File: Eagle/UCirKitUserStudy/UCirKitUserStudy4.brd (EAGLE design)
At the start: 104.1 x 146.3 mm, 30 parts, among them IC1 74595DIL16-OVAL-PIN, IC2 LM35TO92-EXPANDED-OVAL-PIN

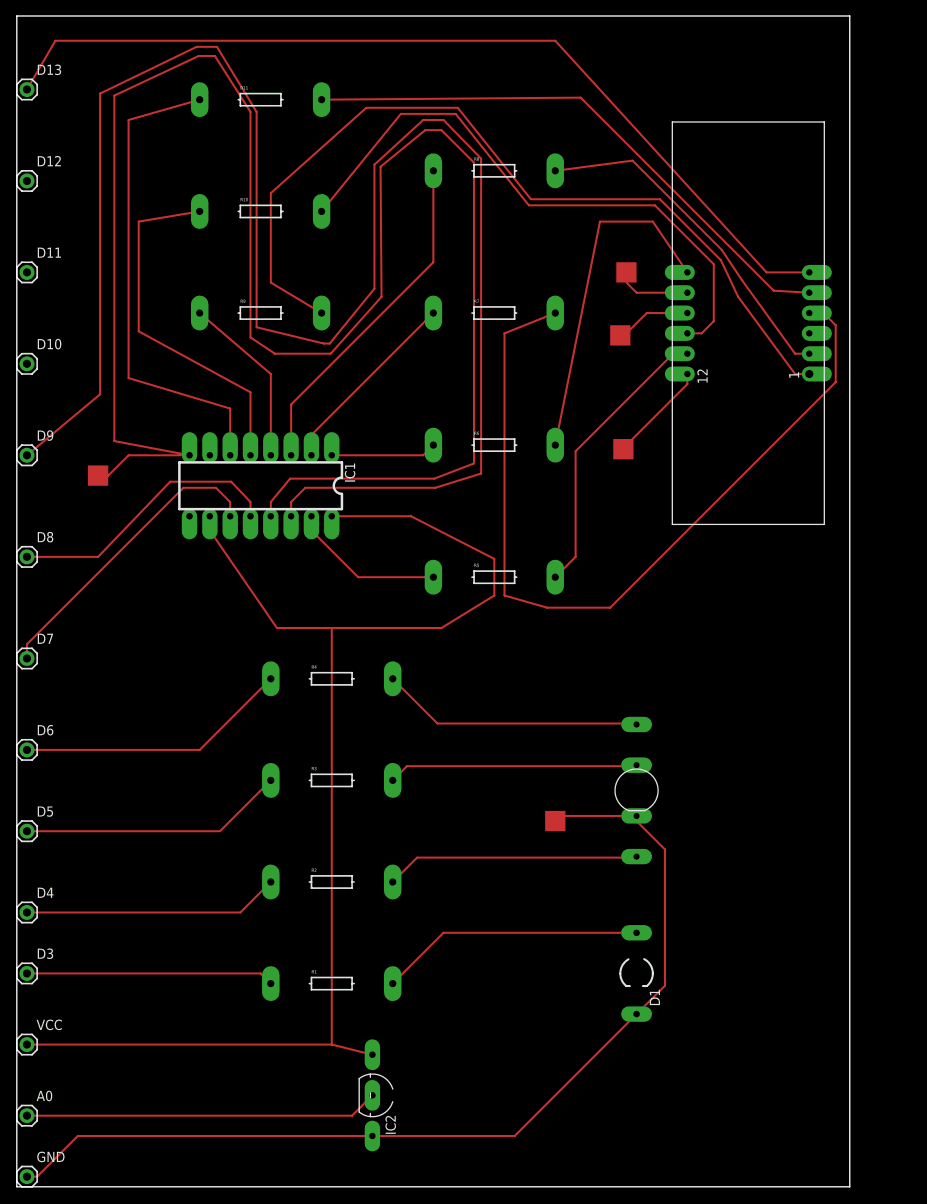
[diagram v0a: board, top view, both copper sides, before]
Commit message: UCirKitUserStudy5 has SMD version of resistor, LED, and RGBLED. UCirKitUserStudy4 has oval shape for jumpers.
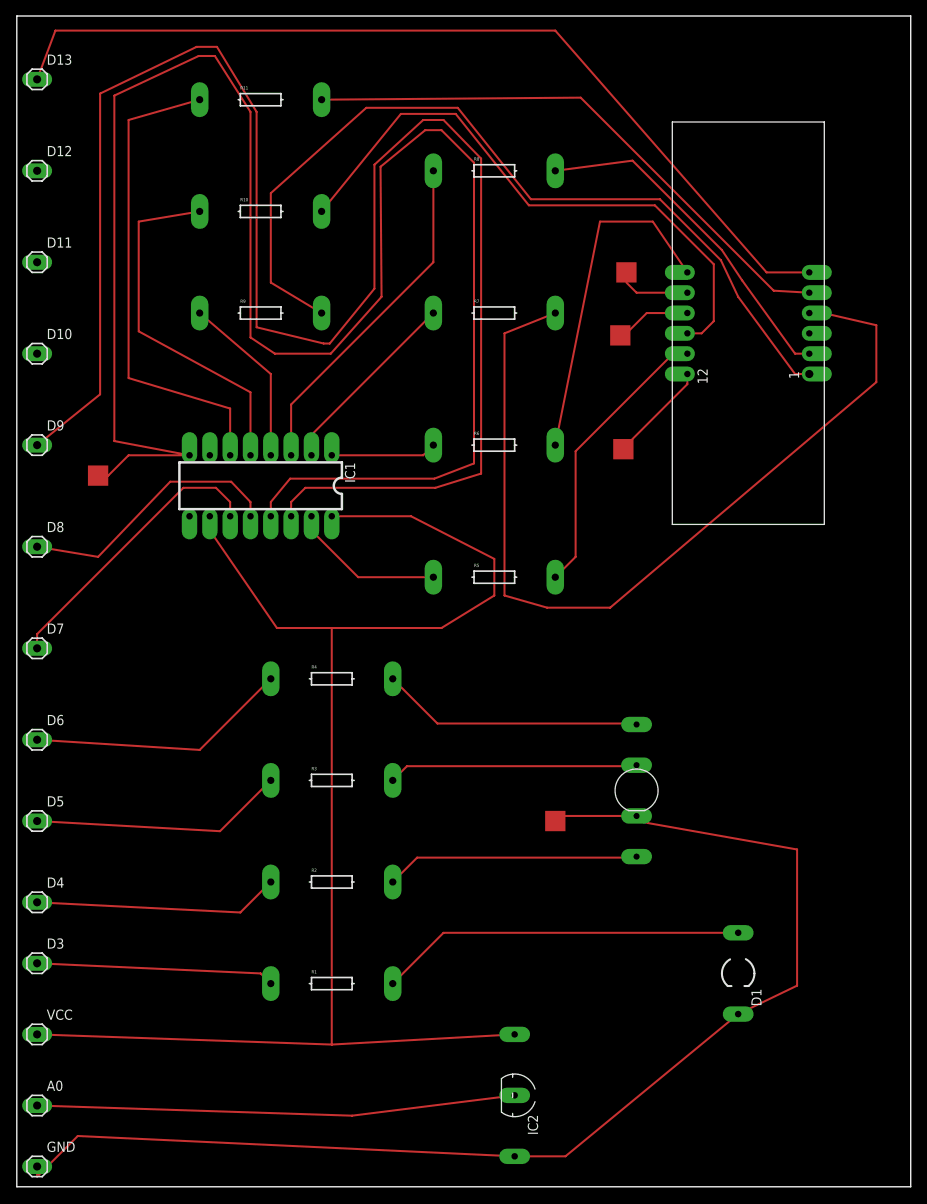
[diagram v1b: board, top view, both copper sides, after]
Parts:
- A0, D10, D11, D12, D13, D3, D4, D5, D6, D7, D8, D9, GND, VCC: device SparkFun-Connectors:1X01 -> SparkFun-Connectors:1X01_OVAL_PIN
- moved IC2 17.8 mm to (62.2, 11.4)
- moved D1 12.7 mm to (90.2, 26.7)
- moved D13 1.80 mm to (2.54, 138.4)
- moved D8 1.80 mm to (2.54, 80.0)
- moved D4 1.80 mm to (2.54, 35.6)
- moved D6 1.80 mm to (2.54, 55.9)
- moved GND 1.80 mm to (2.54, 2.54)
- moved A0 1.80 mm to (2.54, 10.2)
- moved D3 1.80 mm to (2.54, 27.9)
- moved VCC 1.80 mm to (2.54, 19.1)
- moved D10 1.80 mm to (2.54, 104.1)
- moved D11 1.80 mm to (2.54, 115.6)
- moved D12 1.80 mm to (2.54, 127.0)
- moved D5 1.80 mm to (2.54, 45.7)
- moved D7 1.80 mm to (2.54, 67.3)
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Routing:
- net GND: track 356.1 -> 387.4 mm
- net VCC: track 166.5 -> 182.9 mm
- net A0: track 44.2 -> 59.9 mm
- net N$1: track 33.1 -> 45.8 mm
- net N$7: track 103.9 -> 112.3 mm
- net D7: track 37.8 -> 36.0 mm
- net D9: track 219.1 -> 217.3 mm
- net D3: track 31.0 -> 29.8 mm
- net D4: track 32.1 -> 30.8 mm
- net D5: track 33.1 -> 31.9 mm
- net D6: track 34.2 -> 32.9 mm
- net D8: track 34.8 -> 33.7 mm
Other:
- board size 104.1 x 146.3 mm -> 111.7 x 146.3 mm
